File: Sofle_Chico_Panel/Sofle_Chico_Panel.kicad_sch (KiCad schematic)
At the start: 0 parts

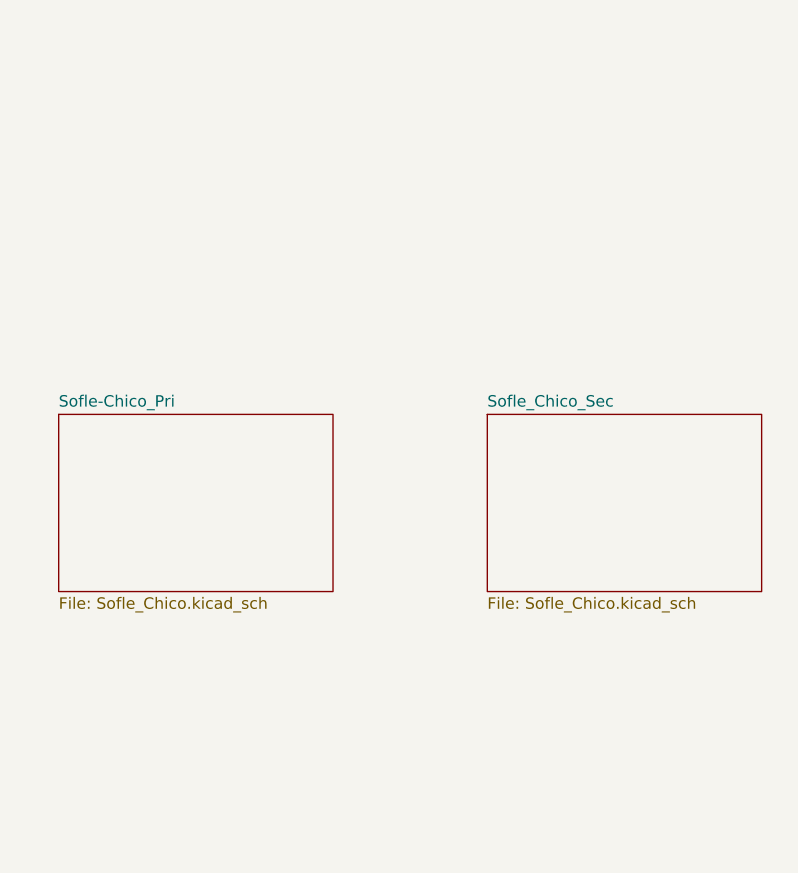
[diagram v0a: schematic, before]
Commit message: Reworked as "batwing" with single-controller connections and no mid-slot to sneak it past JLCPCB.  Singulating will be manual, but lets you get 5 boards with diodes preinstalled
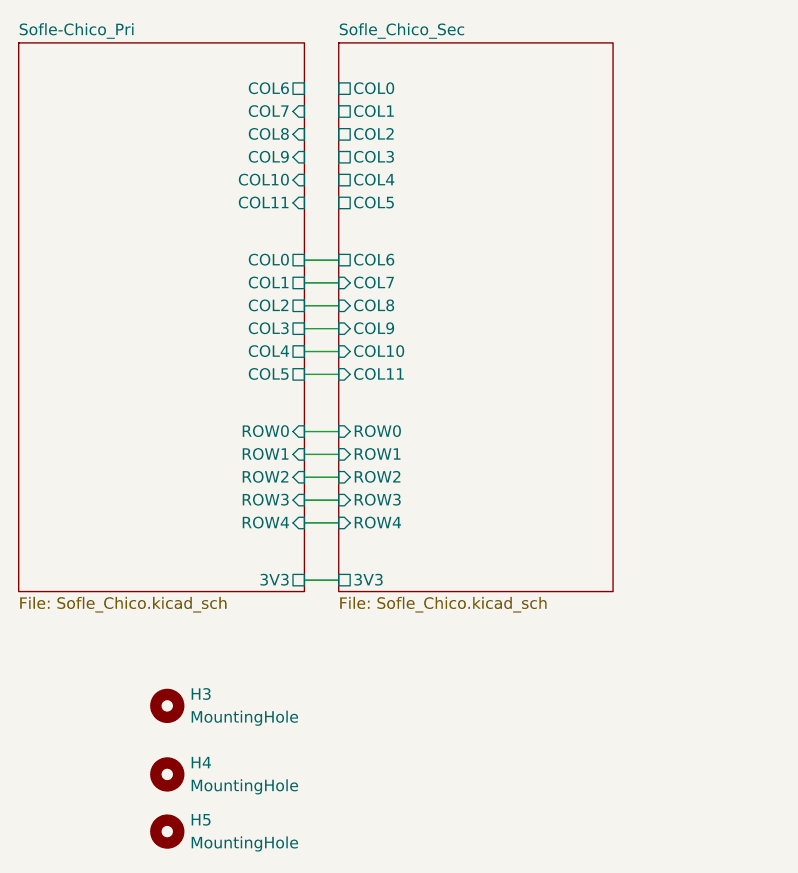
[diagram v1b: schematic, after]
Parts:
- added H3, H4, H5: MountingHole, MountingHole:MountingHole_3.2mm_M3, symbol Mechanical:MountingHole
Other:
- sheet Sofle-Chico_Pri ports: added 3V3, COL0, COL1, COL10, COL11, COL2, COL3, COL4, COL5, COL6, COL7, COL8, COL9, ROW0, ROW1, ROW2, ROW3, ROW4; removed none
- sheet Sofle_Chico_Sec ports: added 3V3, COL0, COL1, COL10, COL11, COL2, COL3, COL4, COL5, COL6, COL7, COL8, COL9, ROW0, ROW1, ROW2, ROW3, ROW4; removed none
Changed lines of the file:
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@@
 (kicad_sch (version 20230121) (generator eeschema)
   (paper "A4")
-  (sheet (at 75.565 79.375) (size 30.48 19.685) (fields_autoplaced)
+  (wire (pts (xy 102.87 69.85) (xy 106.68 69.85))
+    (stroke (width 0) (type default))
+  )
+  (wire (pts (xy 102.87 83.82) (xy 106.68 83.82))
+    (stroke (width 0) (type default))
+  )
+  (wire (pts (xy 102.87 67.31) (xy 106.68 67.31))
+    (stroke (width 0) (type default))
+  )
+  (wire (pts (xy 102.87 74.93) (xy 106.68 74.93))
+    (stroke (width 0) (type default))
+  )
+  (wire (pts (xy 102.87 62.23) (xy 106.68 62.23))
+    (stroke (width 0) (type default))
+  )
+  (wire (pts (xy 102.87 97.79) (xy 106.68 97.79))
+    (stroke (width 0) (type default))
+  )
+  (wire (pts (xy 102.87 86.36) (xy 106.68 86.36))
+    (stroke (width 0) (type default))
+  )
+  (wire (pts (xy 102.87 88.9) (xy 106.68 88.9))
+    (stroke (width 0) (type default))
+  )
+  (wire (pts (xy 102.87 81.28) (xy 106.68 81.28))
+    (stroke (width 0) (type default))
+  )
+  (wire (pts (xy 102.87 64.77) (xy 106.68 64.77))
+    (stroke (width 0) (type default))
+  )
+  (wire (pts (xy 102.87 91.44) (xy 106.68 91.44))
+    (stroke (width 0) (type default))
+  )
+  (wire (pts (xy 102.87 72.39) (xy 106.68 72.39))
+    (stroke (width 0) (type default))
+  )
+  (symbol (lib_id "Mechanical:MountingHole") (at 87.63 111.76 0) (unit 1)
+    (in_bom yes) (on_board yes) (dnp no) (fields_autoplaced)
+    (property "Reference" "H3" (at 90.17 110.49 0)
+      (effects (font (size 1.27 1.27)) (justify left))
+    )
+    (property "Value" "MountingHole" (at 90.17 113.03 0)
+      (effects (font (size 1.27 1.27)) (justify left))
+    )
+    (property "Footprint" "MountingHole:MountingHole_3.2mm_M3" (at 87.63 111.76 0)
+      (effects (font (size 1.27 1.27)) hide)
+    )
+    (property "Datasheet" "~" (at 87.63 111.76 0)
+      (effects (font (size 1.27 1.27)) hide)
+    )
+    (instances
+      (project "Sofle_Chico_Panel"
+        (path "/21b17b23-a59f-4931-b84d-3d9b0f18ccb9"
+          (reference "H3") (unit 1)
+        )
+      )
+    )
+  )
+  (symbol (lib_id "Mechanical:MountingHole") (at 87.63 119.38 0) (unit 1)
+    (in_bom yes) (on_board yes) (dnp no) (fields_autoplaced)
+    (property "Reference" "H4" (at 90.17 118.11 0)
+      (effects (font (size 1.27 1.27)) (justify left))
+    )
+    (property "Value" "MountingHole" (at 90.17 120.65 0)
+      (effects (font (size 1.27 1.27)) (justify left))
+    )
+    (property "Footprint" "MountingHole:MountingHole_3.2mm_M3" (at 87.63 119.38 0)
+      (effects (font (size 1.27 1.27)) hide)
+    )
+    (property "Datasheet" "~" (at 87.63 119.38 0)
+      (effects (font (size 1.27 1.27)) hide)
+    )
+    (instances
+      (project "Sofle_Chico_Panel"
+        (path "/21b17b23-a59f-4931-b84d-3d9b0f18ccb9"
+          (reference "H4") (unit 1)
+        )
+      )
+    )
+  )
+  (symbol (lib_id "Mechanical:MountingHole") (at 87.63 125.73 0) (unit 1)
+    (in_bom yes) (on_board yes) (dnp no) (fields_autoplaced)
+    (property "Reference" "H5" (at 90.17 124.46 0)
+      (effects (font (size 1.27 1.27)) (justify left))
+    )
+    (property "Value" "MountingHole" (at 90.17 127 0)
+      (effects (font (size 1.27 1.27)) (justify left))
+    )
+    (property "Footprint" "MountingHole:MountingHole_3.2mm_M3" (at 87.63 125.73 0)
+      (effects (font (size 1.27 1.27)) hide)
+    )
+    (property "Datasheet" "~" (at 87.63 125.73 0)
+      (effects (font (size 1.27 1.27)) hide)
+    )
+    (instances
+      (project "Sofle_Chico_Panel"
+        (path "/21b17b23-a59f-4931-b84d-3d9b0f18ccb9"
+          (reference "H5") (unit 1)
+        )
+      )
+    )
+  )
+  (sheet (at 71.12 38.1) (size 31.75 60.96) (fields_autoplaced)
     (stroke (width 0.1524) (type solid))
     (fill (color 0 0 0 0.0000))
-    (property "Sheetname" "Sofle-Chico_Pri" (at 75.565 78.6634 0)
+    (property "Sheetname" "Sofle-Chico_Pri" (at 71.12 37.3884 0)
       (effects (font (size 1.27 1.27)) (justify left bottom))
     )
-    (property "Sheetfile" "Sofle_Chico.kicad_sch" (at 75.565 99.6446 0) (show_name)
+    (property "Sheetfile" "Sofle_Chico.kicad_sch" (at 71.12 99.6446 0) (show_name)
       (effects (font (size 1.27 1.27)) (justify left top))
     )
+    (pin "ROW2" input (at 102.87 86.36 0)
+      (effects (font (size 1.27 1.27)) (justify right))
+    )
+    (pin "ROW3" input (at 102.87 88.9 0)
+      (effects (font (size 1.27 1.27)) (justify right))
+    )
+    (pin "ROW4" input (at 102.87 91.44 0)
+      (effects (font (size 1.27 1.27)) (justify right))
+    )
+    (pin "COL6" passive (at 102.87 43.18 0)
+      (effects (font (size 1.27 1.27)) (justify right))
+    )
+    (pin "COL7" input (at 102.87 45.72 0)
+      (effects (font (size 1.27 1.27)) (justify right))
+    )
+    (pin "COL8" input (at 102.87 48.26 0)
+      (effects (font (size 1.27 1.27)) (justify right))
+    )
+    (pin "ROW1" input (at 102.87 83.82 0)
+      (effects (font (size 1.27 1.27)) (justify right))
+    )
+    (pin "ROW0" input (at 102.87 81.28 0)
+      (effects (font (size 1.27 1.27)) (justify right))
+    )
+    (pin "COL11" input (at 102.87 55.88 0)
+      (effects (font (size 1.27 1.27)) (justify right))
+    )
+    (pin "COL10" input (at 102.87 53.34 0)
+      (effects (font (size 1.27 1.27)) (justify right))
+    )
+    (pin "COL9" input (at 102.87 50.8 0)
+      (effects (font (size 1.27 1.27)) (justify right))
+    )
+    (pin "COL5" passive (at 102.87 74.93 0)
+      (effects (font (size 1.27 1.27)) (justify right))
+    )
+    (pin "COL0" passive (at 102.87 62.23 0)
+      (effects (font (size 1.27 1.27)) (justify right))
+    )
+    (pin "COL1" passive (at 102.87 64.77 0)
+      (effects (font (size 1.27 1.27)) (justify right))
+    )
+    (pin "COL2" passive (at 102.87 67.31 0)
+      (effects (font (size 1.27 1.27)) (justify right))
+    )
+    (pin "COL3" passive (at 102.87 69.85 0)
+      (effects (font (size 1.27 1.27)) (justify right))
+    )
+    (pin "COL4" passive (at 102.87 72.39 0)
+      (effects (font (size 1.27 1.27)) (justify right))
+    )
+    (pin "3V3" passive (at 102.87 97.79 0)
+      (effects (font (size 1.27 1.27)) (justify right))
+    )
     (instances
       (project "Sofle_Chico_Panel"
@@
     )
   )
-  (sheet (at 123.19 79.375) (size 30.48 19.685) (fields_autoplaced)
+  (sheet (at 106.68 38.1) (size 30.48 60.96) (fields_autoplaced)
     (stroke (width 0.1524) (type solid))
     (fill (color 0 0 0 0.0000))
-    (property "Sheetname" "Sofle_Chico_Sec" (at 123.19 78.6634 0)
+    (property "Sheetname" "Sofle_Chico_Sec" (at 106.68 37.3884 0)
       (effects (font (size 1.27 1.27)) (justify left bottom))
     )
-    (property "Sheetfile" "Sofle_Chico.kicad_sch" (at 123.19 99.6446 0) (show_name)
+    (property "Sheetfile" "Sofle_Chico.kicad_sch" (at 106.68 99.6446 0) (show_name)
       (effects (font (size 1.27 1.27)) (justify left top))
     )
-    (instances
+    (pin "ROW2" input (at 106.68 86.36 180)
+      (effects (font (size 1.27 1.27)) (justify left))
+    )
+    (pin "ROW3" input (at 106.68 88.9 180)
+      (effects (font (size 1.27 1.27)) (justify left))
+    )
+    (pin "ROW4" input (at 106.68 91.44 180)
+      (effects (font (size 1.27 1.27)) (justify left))
+    )
+    (pin "COL6" passive (at 106.68 62.23 180)
+      (effects (font (size 1.27 1.27)) (justify left))
+    )
+    (pin "COL7" input (at 106.68 64.77 180)
+      (effects (font (size 1.27 1.27)) (justify left))
+    )
+    (pin "COL8" input (at 106.68 67.31 180)
+      (effects (font (size 1.27 1.27)) (justify left))
+    )
+    (pin "ROW1" input (at 106.68 83.82 180)
+      (effects (font (size 1.27 1.27)) (justify left))
+    )
+    (pin "ROW0" input (at 106.68 81.28 180)
+      (effects (font (size 1.27 1.27)) (justify left))
+    )
+    (pin "COL11" input (at 106.68 74.93 180)
+      (effects (font (size 1.27 1.27)) (justify left))
+    )
+    (pin "COL10" input (at 106.68 72.39 180)
+      (effects (font (size 1.27 1.27)) (justify left))
+    )
+    (pin "COL9" input (at 106.68 69.85 180)
+      (effects (font (size 1.27 1.27)) (justify left))
+    )
+    (pin "COL5" passive (at 106.68 55.88 180)
+      (effects (font (size 1.27 1.27)) (justify left))
+    )
+    (pin "COL0" passive (at 106.68 43.18 180)
+      (effects (font (size 1.27 1.27)) (justify left))
+    )
+    (pin "COL1" passive (at 106.68 45.72 180)
+      (effects (font (size 1.27 1.27)) (justify left))
+    )
+    (pin "COL2" passive (at 106.68 48.26 180)
+      (effects (font (size 1.27 1.27)) (justify left))
+    )
+    (pin "COL3" passive (at 106.68 50.8 180)
+      (effects (font (size 1.27 1.27)) (justify left))
+    )
+    (pin "COL4" passive (at 106.68 53.34 180)
+      (effects (font (size 1.27 1.27)) (justify left))
+    )
+    (pin "3V3" passive (at 106.68 97.79 180)
+      (effects (font (size 1.27 1.27)) (justify left))
+    )
+    (instances
